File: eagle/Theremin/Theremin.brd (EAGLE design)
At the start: 161 x 101.6 mm, 70 parts, among them Q8 2N3904, U1 LM78L12, U2 LM79L12

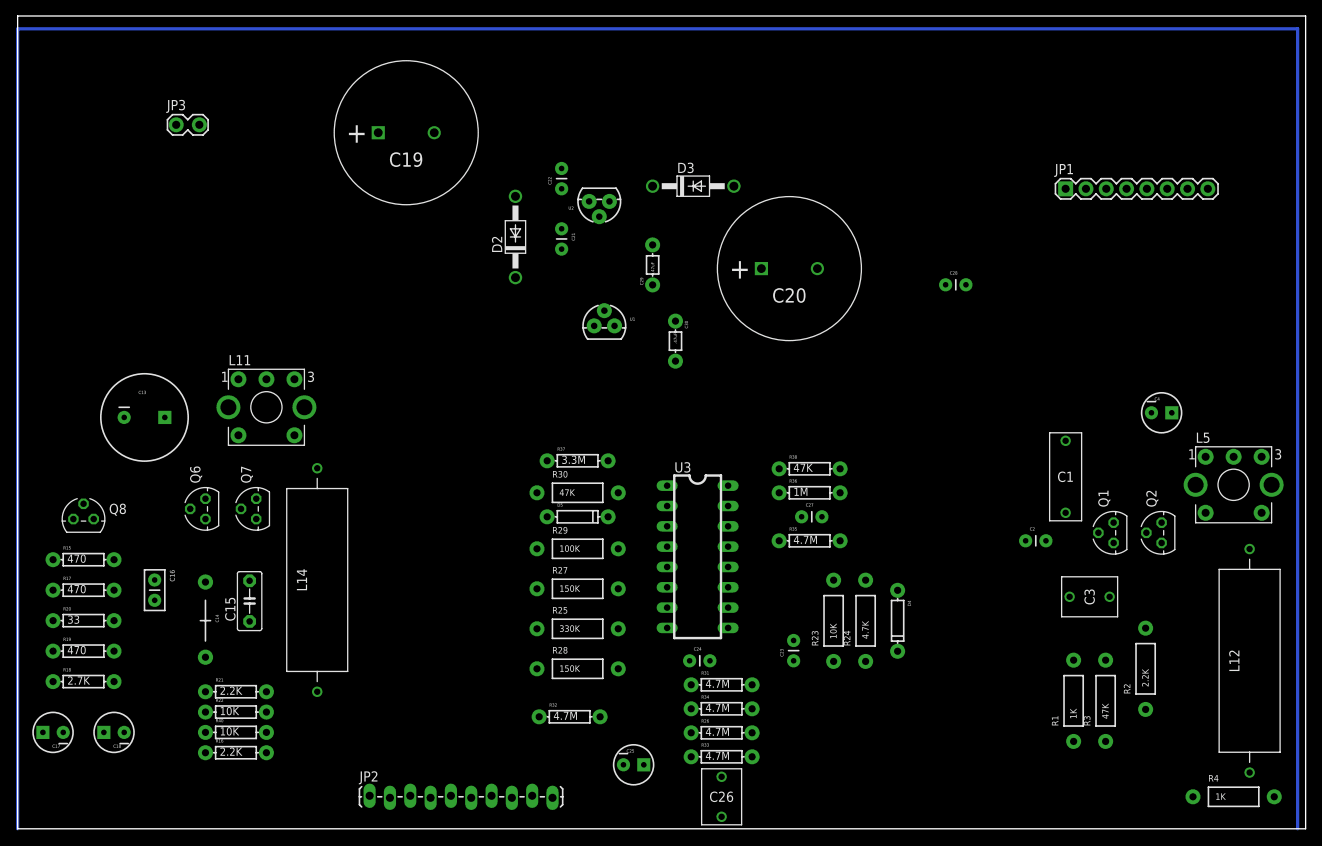
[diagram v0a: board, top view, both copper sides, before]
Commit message: Add the FIXED PITCH OSCILLATOR curcuit
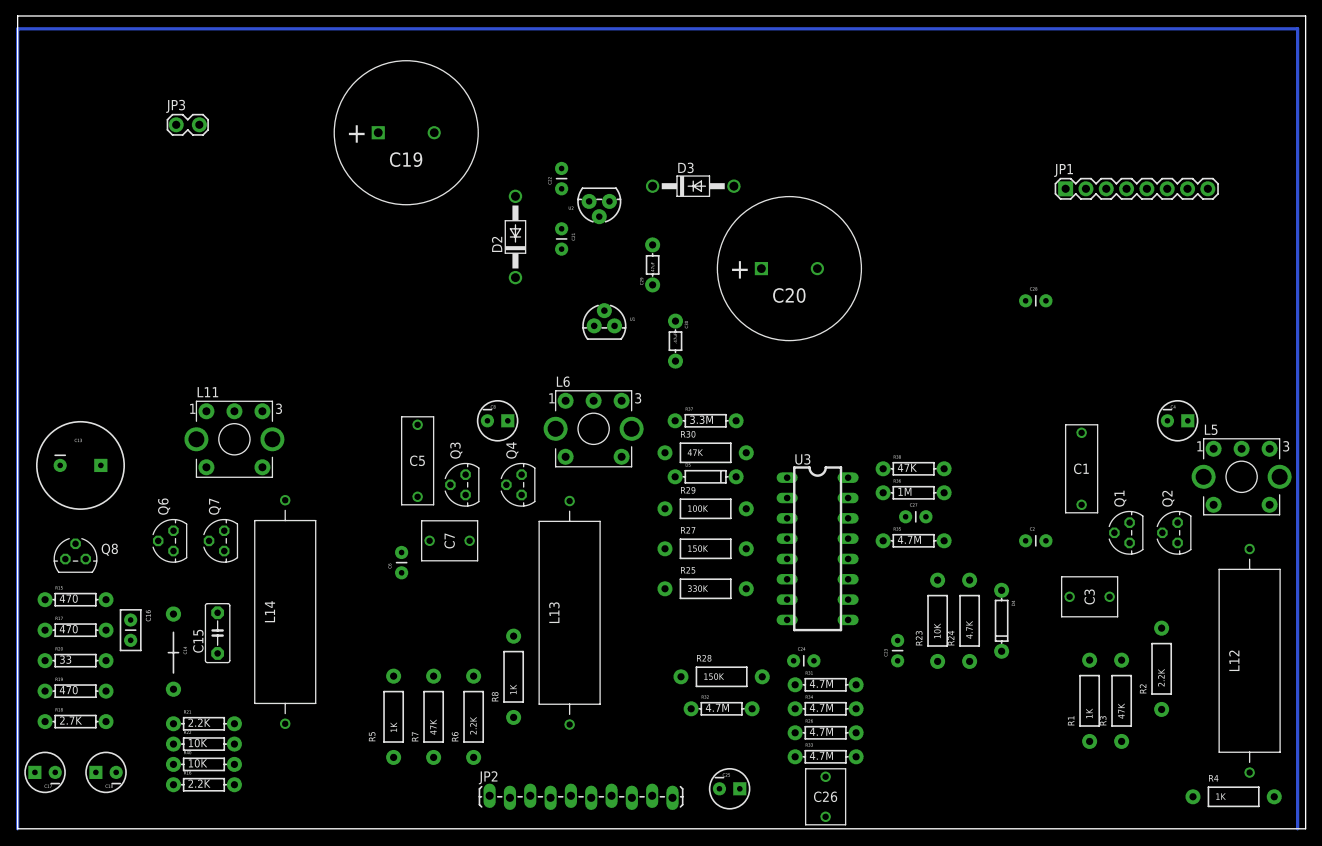
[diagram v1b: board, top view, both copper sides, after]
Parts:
- added C5: 3300pF, marky-parts:9M-CAP-RADIAL
- added C6: 15pF, SparkFun-Capacitors:CAP-PTH-SMALL
- added C7: 0.01uF, marky-parts:5M-CAP-RADIAL
- added C8: 1uF, SparkFun-Passives:CPOL-RADIAL-10UF-25V
- added L13: 47uH, marky-parts:FIXED-INDUCTOR-API-DELEVAN
- added L6: 47uH, marky-parts:SLOT-TEN
- added Q3, Q4: (no value), transistor:TO92
- added R5, R8: 1K, SparkFun-Resistors:AXIAL-0.4
- added R6: 2.2K, SparkFun-Resistors:AXIAL-0.4
- added R7: 47K, SparkFun-Resistors:AXIAL-0.4
- moved R32 19.0 mm to (88.0, 15.0)
- moved R28 18.0 mm to (88.0, 19.0)
- moved D5 16.8 mm to (86.0, 44.0)
- moved R25 16.8 mm to (86.0, 30.0)
- moved R27 16.8 mm to (86.0, 35.0)
- moved R29 16.8 mm to (86.0, 40.0)
- moved R30 16.8 mm to (86.0, 47.0)
- moved R37 16.8 mm to (86.0, 51.0)
- moved U3 15.0 mm to (100.0, 35.0)
- moved JP2 15.0 mm to (59.0, 4.00)
- moved C23 13.0 mm to (110.0, 21.0)
- moved C24 13.0 mm to (97.0, 21.0)
- moved C26 13.0 mm to (101.0, 4.00)
- moved C27 13.0 mm to (111.0, 39.0)
- moved D4 13.0 mm to (123.0, 26.0)
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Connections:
- new net N$40: C3.P$2, R3.P$2
- new net N$41: C5.P$2, C6.1, C7.P$1, L13.P$2, Q3.1
- new net N$42: Q3.2, R5.P$1
- new net N$43: Q3.3, Q4.3, R6.P$2
- new net N$44: L13.P$1, L6.OUT$3
- new net N$46: C7.P$2, R7.P$2
- new net N$48: Q4.2, R7.P$1, R8.P$1
- net 5V: now also C5.P$1, C8.1, L6.IN$1, Q4.1; no longer C3.P$2, R3.P$2
- net GND: now also C8.2, L6.TAB@7, L6.TAB@8, R5.P$2, R8.P$2
- net N$20: now also C6.2
- net VNEG: now also R6.P$1

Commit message: Add PITCH TUNING curcuit
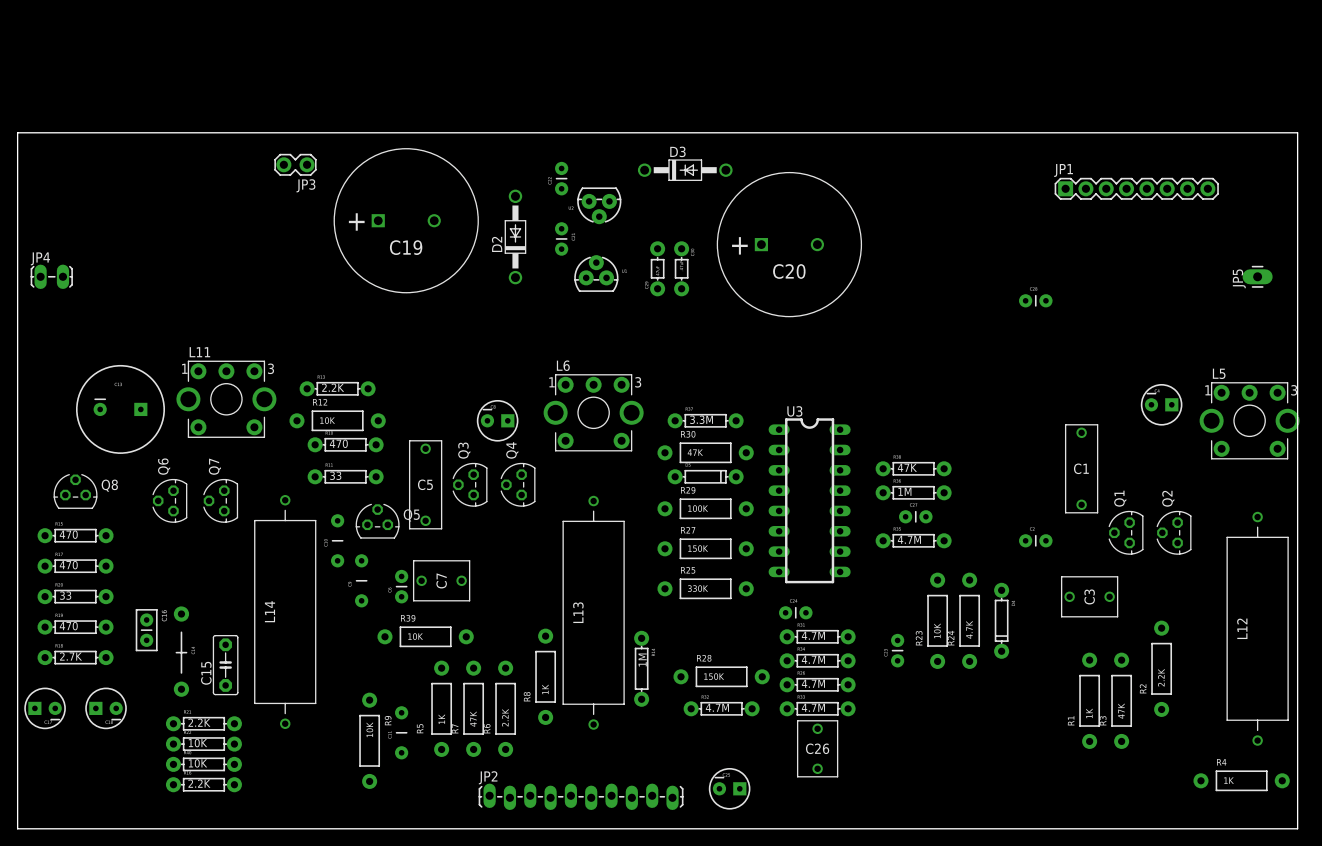
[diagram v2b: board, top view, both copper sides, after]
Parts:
- added C10, C11, C9: 0.47uF, SparkFun-Capacitors:CAP-PTH-5MM
- added JP4: VOL_ANT, SparkFun-Connectors:1X02_LOCK_LONGPADS
- added JP5: PITCH_ANT, SparkFun-Connectors:1X01_LONGPAD
- added Q5: (no value), transistor:TO92
- added R10: 470, SparkFun-Passives:AXIAL-0.3EZ
- added R11: 33, SparkFun-Passives:AXIAL-0.3EZ
- added R12, R39, R9: 10K, SparkFun-Resistors:AXIAL-0.4
- added R13: 2.2K, SparkFun-Passives:AXIAL-0.3EZ
- added R14: 1M, SparkFun-Passives:AXIAL-0.3EZ
- moved JP3 16.8 mm to (36.0, 83.0), turned to 180 degrees
- moved C19 11.0 mm to (48.6, 76.0)
- moved C30 9.07 mm to (83.0, 70.0)
- moved C13 8.60 mm to (12.9, 52.4)
- moved C17 8.00 mm to (3.43, 15.1)
- moved C18 8.00 mm to (11.1, 15.1)
- moved Q8 8.00 mm to (7.24, 41.7)
- moved R15 8.00 mm to (7.24, 36.6)
- moved R17 8.00 mm to (7.24, 32.8)
- moved R19 8.00 mm to (7.24, 25.2)
- moved R20 8.00 mm to (7.24, 29.0)
- moved R18 8.00 mm to (7.24, 21.4)
- moved L5 7.07 mm to (154.0, 51.0)
- moved C24 6.08 mm to (96.0, 27.0)
- moved C26 6.08 mm to (100.0, 10.0)
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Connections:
- new net N$15: JP4.2, R14.P$2
- new net N$45: C10.1, C11.2, Q5.3, R39.P$1, R9.P$1
- new net N$47: JP2.5, R9.P$2
- new net N$49: Q5.2, R10.P$2
- new net N$50: C9.2, R10.P$1, R11.P$2
- new net N$51: C10.2, R11.P$1, R12.P$1, R13.P$2
- net 5V: now also C11.1
- net GND: now also R13.P$1
- net N$17: now also JP5.1
- net N$26: now also R14.P$1
- net N$41: now also C9.1, Q5.1
- net N$9: now also JP4.1
- net VNEG: now also R12.P$2, R39.P$2
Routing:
- net N$15: track 360.0 -> 0.00 mm
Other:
- board size 161 x 101.6 mm -> 160 x 87 mm
- board text added: "DETECTOR, VCA & PROCESSOR"
- board text added: "FIXED PITCH OSC & TUNING"
- board text added: "Marky's House THEREMIN"
- board text added: "VAR PITCH OSC"
- board text removed: "Marky's House"

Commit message: Add jumper and resistor for selecting output amp type
Normal (keyboard, stereo) and Guitar / Bass
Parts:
- removed R33: 4.7M, SparkFun-Passives:AXIAL-0.3EZ
- added AMP-SELECT: (no value), SparkFun-Connectors:1X03_LOCK_LONGPADS
- added JP6: C28_SHORT, SparkFun-Connectors:1X02_LOCK
- added R33A: 4.7K, SparkFun-Passives:AXIAL-0.3EZ
- added R33B: 47K, SparkFun-Passives:AXIAL-0.3EZ
- R26, R31, R32, R34: value 4.7M -> 4.7K
- moved L5 2.24 mm to (152.0, 52.0)
- moved C26 2.00 mm to (100.0, 8.00)
- moved C4 2.00 mm to (141.0, 53.0)
- moved C24 1.00 mm to (96.0, 28.0)
- moved R1 1.00 mm to (133.0, 16.0)
- moved R26 1.00 mm to (100.0, 19.0)
- moved R31 1.00 mm to (100.0, 25.0)
- moved R34 1.00 mm to (100.0, 22.0)
- moved R4 1.00 mm to (152.0, 6.00)
- moved U3 1.00 mm to (99.0, 42.0)
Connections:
- removed net N$31: C26.P$2, JP2.10, R33.P$2, R34.P$1
- new net N$52: AMP-SELECT.3, R33A.P$1
- new net N$53: AMP-SELECT.1, R33B.P$1
- new net N$54: C26.P$2, JP2.10, R33A.P$2, R33B.P$2, R34.P$1
- net GND: now also JP6.2
- net N$24: now also JP6.1
- net N$30: now also AMP-SELECT.2; no longer R33.P$1
- net N$37: now also U3.3
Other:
- board text added: "GUITAR AMP"
- board text added: "NORMAL"

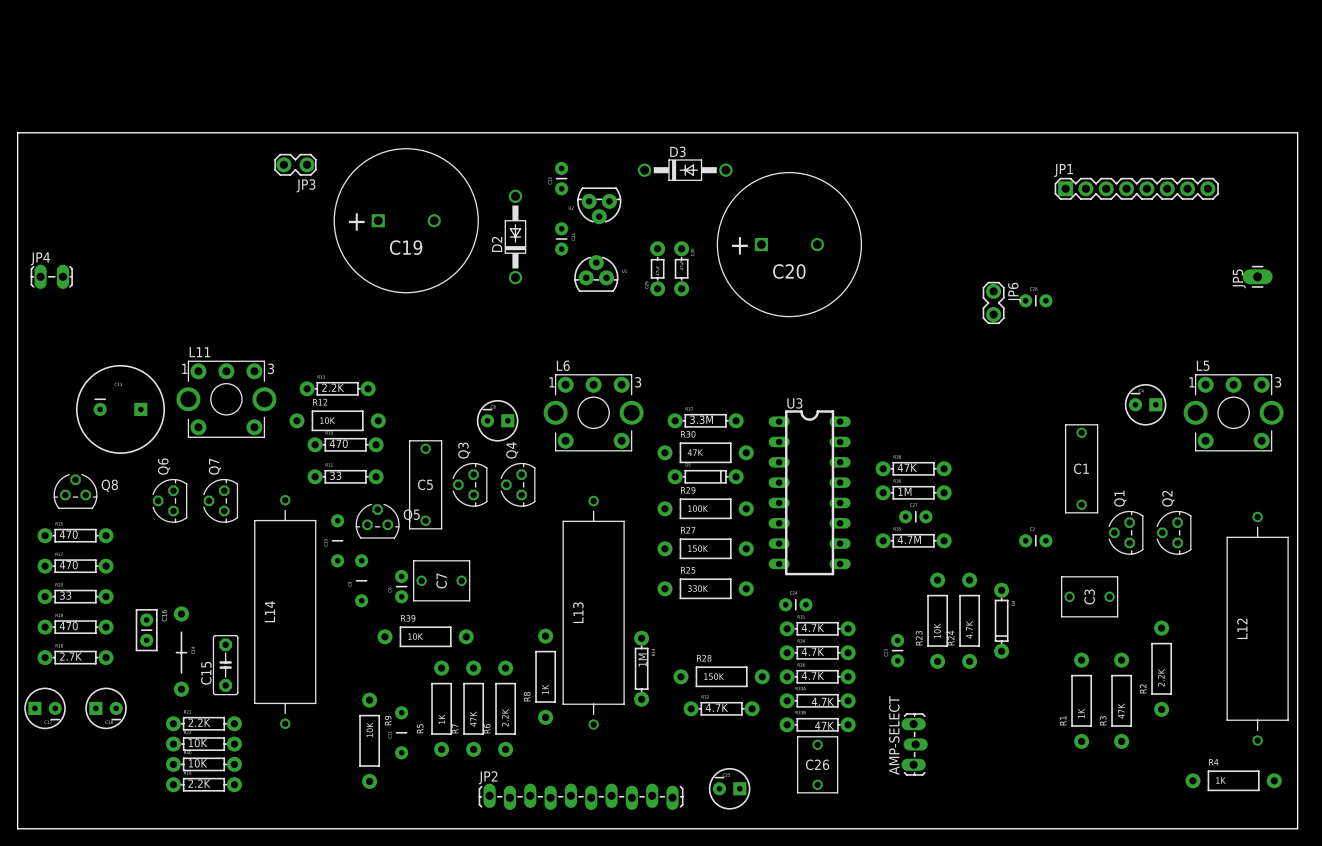
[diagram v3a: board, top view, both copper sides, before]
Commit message: Clean up board layout
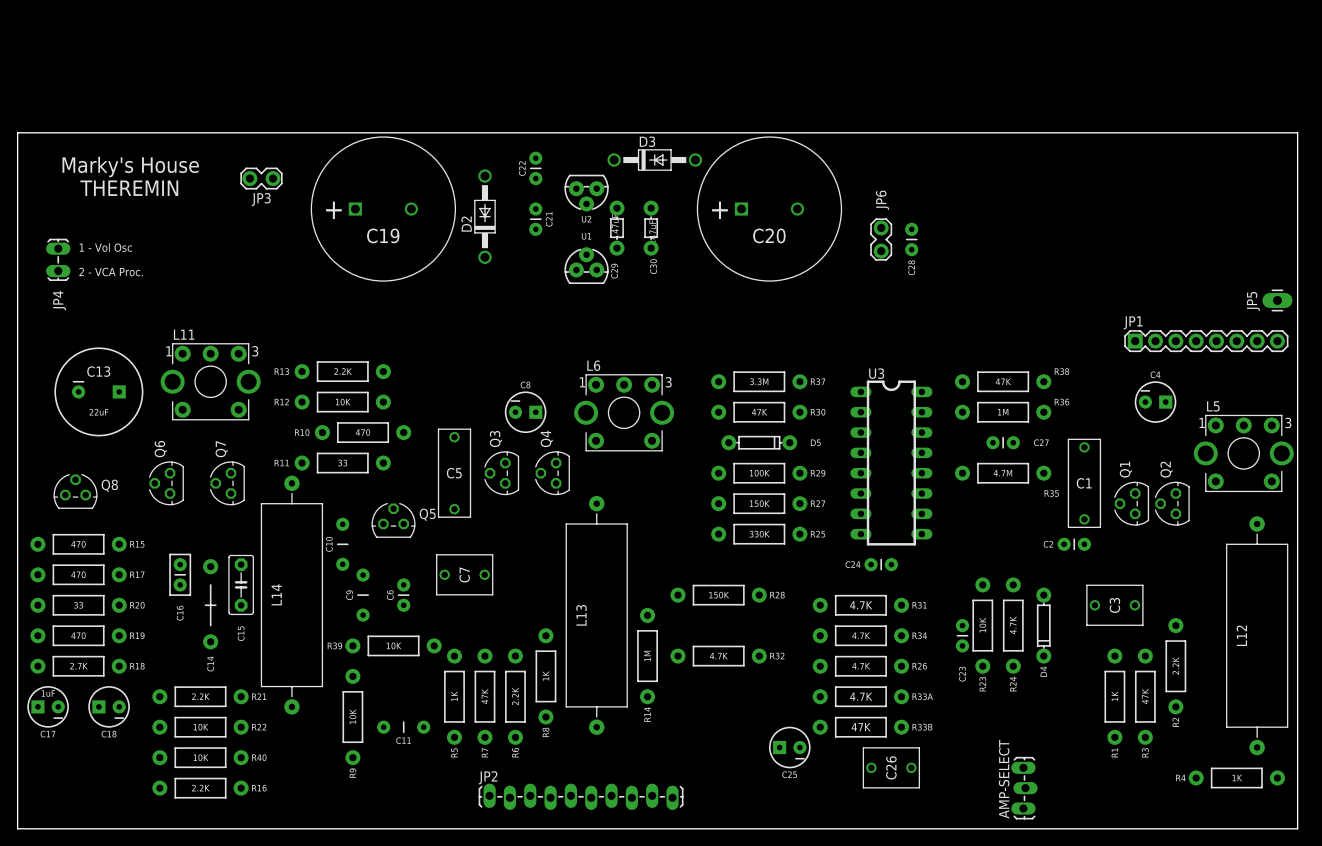
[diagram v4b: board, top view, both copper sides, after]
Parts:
- R10, R11, R13, R14, R15, R16, R17, R18, R19, R20, R21, R22, R26, R31, R32, R33A, R33B, R34, R35, R36, R37, R38, R40: device SparkFun-Passives:AXIAL-0.3EZ -> SparkFun-Resistors:AXIAL-0.4
- moved JP1 20.9 mm to (139.7, 61.0)
- moved JP6 16.1 mm to (108.0, 74.9)
- moved C28 15.6 mm to (111.8, 72.4), turned to 90 degrees
- moved R38 15.6 mm to (123.2, 55.9)
- moved R36 15.1 mm to (123.2, 52.1)
- moved AMP-SELECT 14.8 mm to (125.7, 2.54)
- moved C27 14.3 mm to (121.9, 48.3)
- moved R35 14.0 mm to (123.2, 44.5)
- moved C24 11.8 mm to (106.7, 33.0)
- moved U3 10.9 mm to (109.2, 45.7)
- moved R28 10.2 mm to (87.6, 29.2)
- moved C15 10.2 mm to (27.9, 30.5)
- moved R25 9.57 mm to (92.7, 36.8)
- moved C26 9.23 mm to (109.2, 7.62), turned to 90 degrees
- moved C25 9.12 mm to (96.5, 10.2), turned to 180 degrees
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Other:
- board text added: "1 - Vol Osc 2 - VCA Proc."

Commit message: Add headphone amp
various tweaks
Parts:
- removed AMP-SELECT: (no value), SparkFun-Connectors:1X03_LOCK_LONGPADS
- added C1-H: 0.1uF, SparkFun-Capacitors:CAP-PTH-SMALL
- added IC1-H: TL081, analog-devices:DIL08
- added JP7: HEADPHONE, SparkFun-Connectors:1X03_LOCK_LONGPADS
- added JP8: VOL TUNE, SparkFun-Connectors:1X01_LONGPAD
- added JP9: AMP-SELECT, SparkFun-Connectors:1X03_LOCK_LONGPADS
- added R1-H: 10K, SparkFun-Resistors:AXIAL-0.4
- added R2-H: 100K, SparkFun-Resistors:AXIAL-0.4
- added R3-H, R4-H: 330, SparkFun-Resistors:AXIAL-0.4
- D4, D5: value (none) -> 1N4148
- JP5: device SparkFun-Connectors:1X01_LONGPAD -> SparkFun-Connectors:1X02_LOCK_LONGPADS
- moved JP5 5.24 mm to (156.2, 71.1)
- moved JP3 4.02 mm to (33.0, 77.5), turned to 270 degrees
- moved JP4 1.80 mm to (3.81, 73.7)
- moved L5 1.27 mm to (152.0, 46.9)
- moved JP1 1.27 mm to (139.7, 59.7)
- moved JP2 0.61 mm to (58.4, 3.81)
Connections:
- new net N$31: C1-H.1, IC1-H.3, R1-H.P$2, R2-H.P$1
- new net N$55: C1-H.2, IC1-H.6, R2-H.P$2, R3-H.P$1, R4-H.P$1
- new net N$56: JP7.1, R3-H.P$2
- new net N$57: JP7.2, R4-H.P$2
- net 5V: now also IC1-H.7
- net GND: now also IC1-H.2, JP7.3
- net N$17: now also JP5.2
- net N$24: now also JP8.1
- net N$30: now also JP9.2; no longer AMP-SELECT.2
- net N$52: now also JP9.3; no longer AMP-SELECT.3
- net N$53: now also JP9.1; no longer AMP-SELECT.1
- net N$54: now also R1-H.P$1
- net VNEG: now also IC1-H.4
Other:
- board text added: "GND"
- board text added: "HEADPHONE AMP"

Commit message: Finalized board layout
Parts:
- added JP10, JP11, JP12: (no value), SparkFun-Connectors:1X02_LOCK
- added U$1, U$2, U$3: (no value), marky-parts:GROUND-SCREW
- C1-H: value 0.1uF -> 100pF
- JP1: value (none) -> AUX
- JP2: device SparkFun-Connectors:1X10_LOCK_LONGPADS -> SparkFun-Connectors:1X10
- JP3: device SparkFun-Connectors:1X02_LOCK -> SparkFun-Connectors:1X02_NO_SILK
- JP4: value VOL_ANT -> VOLUME_ANT; device SparkFun-Connectors:1X02_LOCK_LONGPADS -> SparkFun-Connectors:1X02_NO_SILK
- JP5: device SparkFun-Connectors:1X02_LOCK_LONGPADS -> SparkFun-Connectors:1X02_NO_SILK
- JP7: device SparkFun-Connectors:1X03_LOCK_LONGPADS -> SparkFun-Connectors:1X03_NO_SILK
- JP9: device SparkFun-Connectors:1X03_LOCK_LONGPADS -> SparkFun-Connectors:1X03_LOCK
- U3: value (none) -> LM13700N
- moved JP7 14.6 mm to (127.6, 81.9)
- moved D2 10.6 mm to (65.1, 68.3)
- moved C19 9.40 mm to (54.9, 75.6)
- moved JP3 7.68 mm to (40.6, 76.5), turned to 0 degrees
- moved C1-H 6.84 mm to (132.1, 77.5), turned to 180 degrees
- moved R1-H 5.72 mm to (130.8, 74.3)
- moved C29 5.40 mm to (79.7, 72.5), turned to 270 degrees
- moved U2 5.39 mm to (74.9, 76.2)
- moved R2-H 5.08 mm to (130.8, 71.1), turned to 180 degrees
- moved C16 4.62 mm to (19.1, 28.6)
- moved R3-H 4.45 mm to (130.8, 67.9)
- moved JP5 4.02 mm to (154.9, 67.3)
- moved U1 4.02 mm to (74.9, 68.6)
- moved C23 3.86 mm to (117.5, 26.7)
- moved C30 3.82 mm to (82.0, 72.5), turned to 90 degrees
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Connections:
- new net N$58: JP10.2, U$2.P$1
- new net N$59: JP11.2, U$1.P$1
- new net N$60: JP12.2, U$3.P$1
- net GND: now also JP10.1, JP11.1, JP12.1
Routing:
- net GND: track 0.00 -> 643.8 mm
- net 5V: track 0.00 -> 370.6 mm
- net VNEG: track 0.00 -> 319.6 mm
- net -12V: track 0.00 -> 231.2 mm, vias 0 -> 1
- net N$54: track 0.00 -> 123.1 mm
- net N$15: track 0.00 -> 121.8 mm
- net N$20: track 0.00 -> 119.4 mm
- net N$37: track 0.00 -> 116.3 mm, vias 0 -> 1
- net N$17: track 0.00 -> 114.1 mm
- net N$7: track 0.00 -> 106.7 mm
- net N$14: track 0.00 -> 105.6 mm
- net N$41: track 0.00 -> 98.1 mm
- net N$24: track 0.00 -> 88.0 mm
- net N$39: track 0.00 -> 80.0 mm
- net N$26: track 0.00 -> 72.6 mm
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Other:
- board size 160 x 87 mm -> 160 x 86.4 mm
- board text added: "2 - VCA Proc. 1 - Vol Osc"
- board text added: "Marky's House THEREMIN R1"
- board text removed: "1 - Vol Osc 2 - VCA Proc."
- board text removed: "Marky's House THEREMIN"
